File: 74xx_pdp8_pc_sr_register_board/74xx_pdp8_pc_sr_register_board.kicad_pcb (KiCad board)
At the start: 4 copper layers, 137.2 x 88.9 mm, 33 parts, among them P1 DIL24, P2 DIL24, P3 DIL24, P4 DIL24, P5 DIL24, U1 74HC125, U10 74HC04, U11 74HC163, U12 74HC163, U13 74HC163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

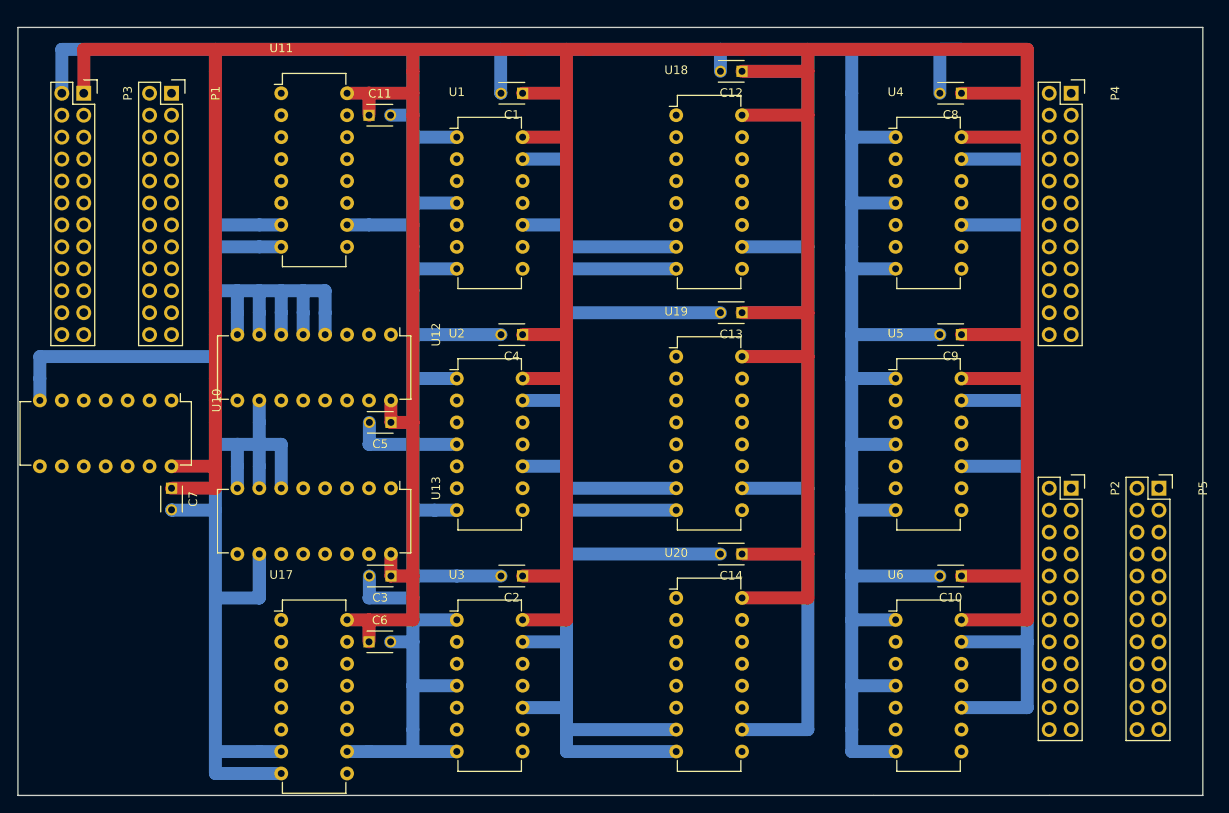
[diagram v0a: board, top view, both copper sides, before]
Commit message: Big changes - elected to switch to board interconnections along one long edge only. Boards to connect to backplane via right-angled DIL connectors. Both register boards and register mux boards thusly modified.
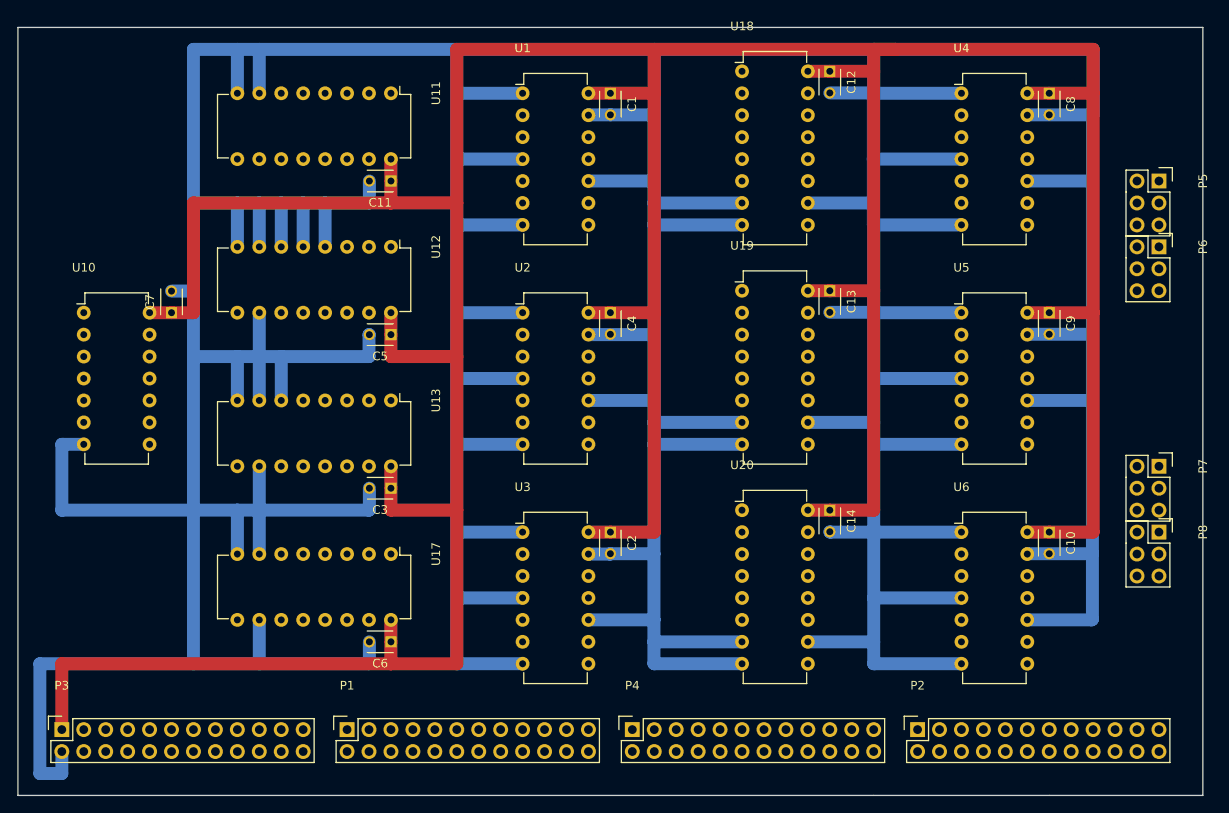
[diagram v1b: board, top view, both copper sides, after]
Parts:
- added P6: DIL6, Socket_Strips:Socket_Strip_Straight_2x03, F.Cu at (149.9, 129.5)
- added P7: DIL6, Socket_Strips:Socket_Strip_Straight_2x03, F.Cu at (149.9, 154.9)
- added P8: DIL6, Socket_Strips:Socket_Strip_Straight_2x03, F.Cu at (149.9, 162.6)
- P5: value DIL24 -> DIL6; footprint Socket_Strips:Socket_Strip_Straight_2x12 -> Socket_Strips:Socket_Strip_Straight_2x03
- moved P4 89.5 mm to (88.9, 185.4), turned to 0 degrees
- moved P1 76.4 mm to (55.9, 185.4), turned to 0 degrees
- moved P3 73.7 mm to (22.9, 185.4), turned to 0 degrees
- moved P5 35.6 mm to (149.9, 121.9)
- moved P2 33.1 mm to (121.9, 185.4), turned to 0 degrees
- moved C7 20.3 mm to (35.6, 137.2), turned to 90 degrees
- moved U17 14.8 mm to (61.0, 165.1), turned to 270 degrees
- moved U10 14.4 mm to (25.4, 137.2), turned to 0 degrees
- moved U11 12.7 mm to (61.0, 111.8), turned to 270 degrees
- moved U3 12.7 mm to (76.2, 162.6)
- moved U6 12.7 mm to (127.0, 162.6)
- moved U20 12.7 mm to (101.6, 160.0)
- moved C14 11.4 mm to (111.8, 160.0), turned to 270 degrees
- moved C10 11.4 mm to (137.2, 162.6), turned to 270 degrees
- moved C2 11.4 mm to (86.4, 162.6), turned to 270 degrees
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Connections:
- P2 pad 12: (no net) -> /OUT_PC_11
- P5 pad 4: /OUT_BUF_PC_3 -> /OUT_BUF_PC_9
- P5 pad 5: /OUT_BUF_PC_4 -> /OUT_BUF_PC_10
- P5 pad 6: /OUT_BUF_PC_5 -> /OUT_BUF_PC_11
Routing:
- net GND: track 1135.8 -> 1036.7 mm
- net (no net): track 91.4 -> 0.00 mm
- net VCC: track 589.3 -> 518.2 mm
- net /OUT_PC_3: track 5.08 -> 7.62 mm
- net /OUT_PC_2: track 5.08 -> 7.62 mm
- net /OUT_PC_1: track 5.08 -> 7.62 mm
- net /OUT_PC_0: track 5.08 -> 7.62 mm
- net /OUT_PC_7: track 5.08 -> 7.62 mm
- net /OUT_PC_6: track 5.08 -> 7.62 mm
- net /OUT_PC_5: track 5.08 -> 7.62 mm
- net /OUT_AC_9: track 5.08 -> 7.62 mm
- net /OUT_AC_8: track 5.08 -> 7.62 mm
- net /OUT_AC_5: track 5.08 -> 7.62 mm
- net /OUT_AC_4: track 5.08 -> 7.62 mm
- net /OUT_AC_1: track 5.08 -> 7.62 mm
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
